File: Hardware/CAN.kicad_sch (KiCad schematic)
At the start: 10 parts, among them J8 Conn_01x02_Pin, U4 TCAN337, U5 CDSOT23-T24CAN

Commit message: small tweaks
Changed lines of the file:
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@@
 	)
 	(hierarchical_label "CAN_LOW"
-		(shape input)
+		(shape bidirectional)
 		(at 29.21 81.28 180)
 		(effects
@@
 	)
 	(hierarchical_label "CAN_LOW"
-		(shape input)
+		(shape bidirectional)
 		(at 63.5 43.18 0)
 		(effects
@@
 	)
 	(hierarchical_label "CAN_LOW"
-		(shape input)
+		(shape bidirectional)
 		(at 76.2 95.25 180)
 		(effects
@@
 	)
 	(hierarchical_label "CAN_HIGH"
-		(shape input)
+		(shape bidirectional)
 		(at 29.21 78.74 180)
 		(effects
@@
 	)
 	(hierarchical_label "CAN_RX"
-		(shape output)
+		(shape bidirectional)
 		(at 34.29 38.1 180)
 		(effects
@@
 	)
 	(hierarchical_label "CAN_TX"
-		(shape input)
+		(shape bidirectional)
 		(at 34.29 35.56 180)
 		(effects
@@
 	)
 	(hierarchical_label "CAN_HIGH"
-		(shape input)
+		(shape bidirectional)
 		(at 76.2 69.85 180)
 		(effects
@@
 	)
 	(hierarchical_label "CAN_TX"
-		(shape input)
+		(shape bidirectional)
 		(at 104.14 74.93 180)
 		(effects
@@
 	)
 	(hierarchical_label "CAN_RX"
-		(shape output)
+		(shape bidirectional)
 		(at 104.14 77.47 180)
 		(effects
@@
 	)
 	(hierarchical_label "CAN_HIGH"
-		(shape input)
+		(shape bidirectional)
 		(at 63.5 38.1 0)
 		(effects

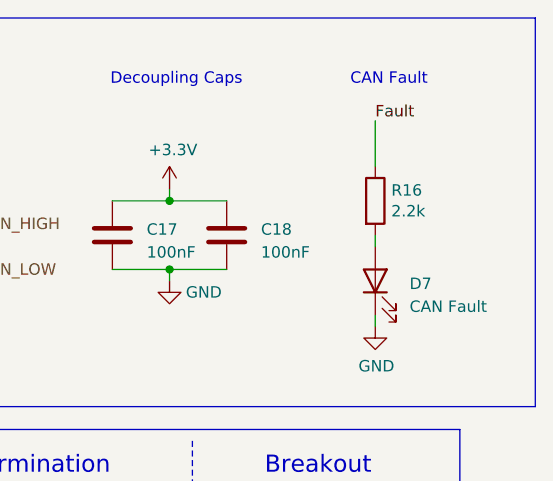
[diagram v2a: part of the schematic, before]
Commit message: new isolated amp, filter stage; need to select values
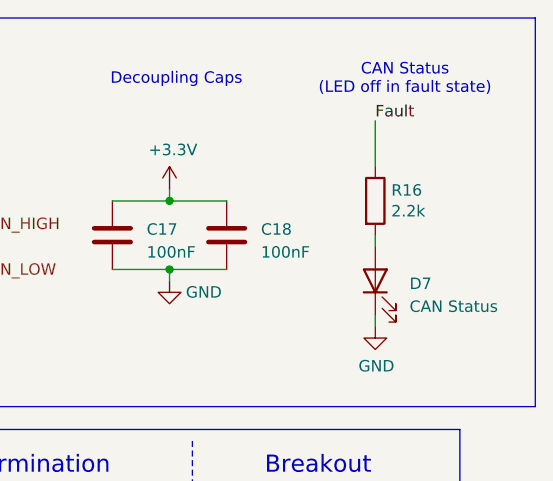
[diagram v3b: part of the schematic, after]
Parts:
- D7: value CAN Fault -> CAN Status
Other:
- note added: "CAN Status (LED off in fault state)"
- note removed: "CAN Fault"
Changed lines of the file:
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@@
 		)
 	)
-	(text "CAN Fault"
+	(text "CAN Status\n(LED off in fault state)"
 		(exclude_from_sim no)
-		(at 110.744 22.098 0)
-		(effects
-			(font
-				(size 1.27 1.27)
-			)
+		(at 112.522 20.32 0)
+		(effects
+			(font
+				(size 1.27 1.27)
+			)
+			(justify top)
 		)
 	)
@@
 			)
 		)
-		(property "Value" "CAN Fault"
+		(property "Value" "CAN Status"
 			(at 113.03 47.3074 90)
 			(effects

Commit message: lowk got some filter values from chat PLEASE PLEASE PLEASE VERIFY LATER
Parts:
- removed D7: CAN Status, LED_SMD:LED_0805_2012Metric, symbol Device:LED
- added D11: CAN Status, symbol Device:LED
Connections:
- net GND: now also D11.1 (K)
- net at R16.2: now also D11.2 (A)

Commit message: plz review
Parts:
- R16: value 2.2k -> ??
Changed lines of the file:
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@@
 			)
 		)
-		(property "Value" "2.2k"
+		(property "Value" "??"
 			(at 110.998 36.703 0)
 			(effects

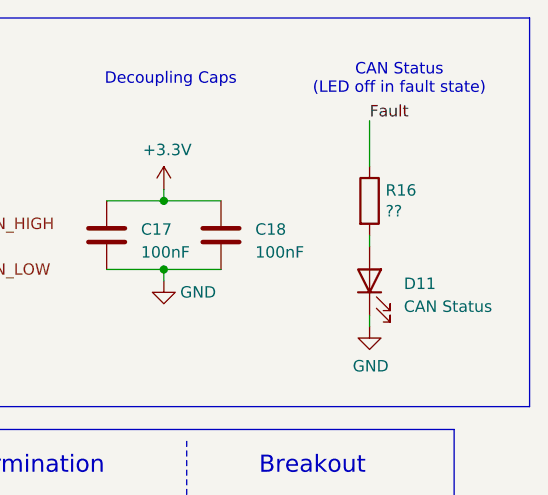
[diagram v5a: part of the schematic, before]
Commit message: added LEDs, changed LDO, still need to address other comments
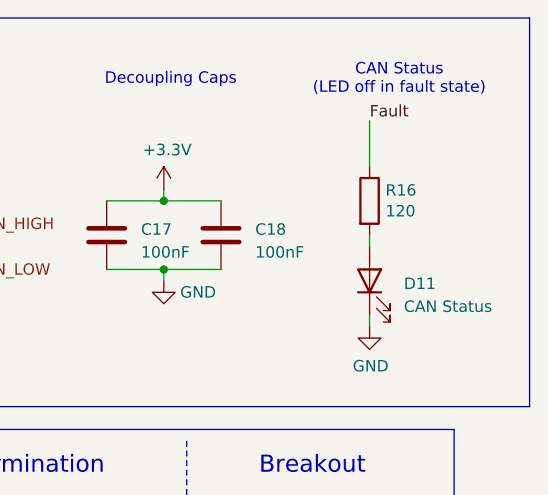
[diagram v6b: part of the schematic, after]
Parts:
- R16: value ?? -> 120
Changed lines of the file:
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@@
 			)
 		)
-		(property "Value" "??"
+		(property "Value" "120"
 			(at 110.998 36.703 0)
 			(effects

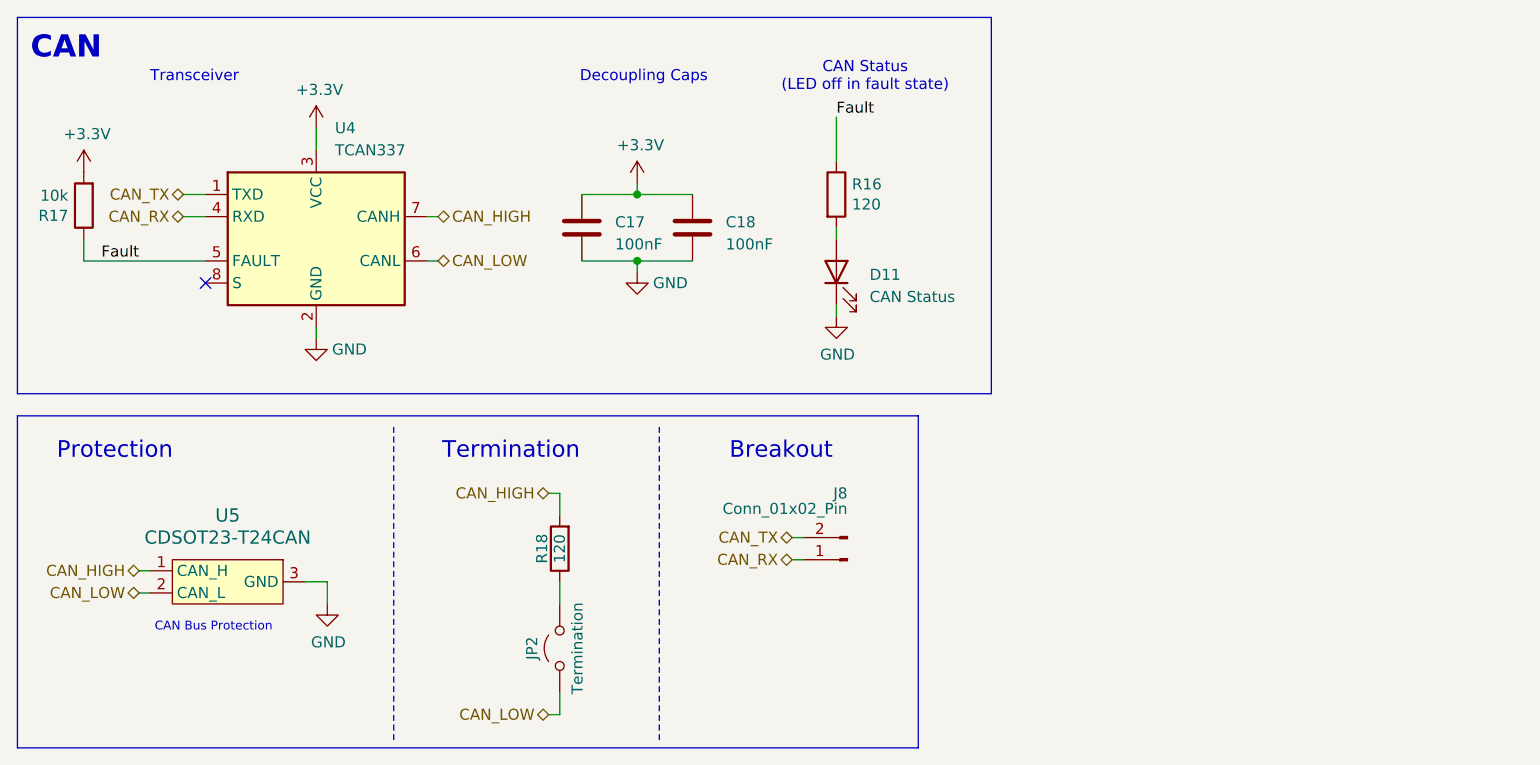
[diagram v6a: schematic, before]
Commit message: scrutineering should be done, started on USB
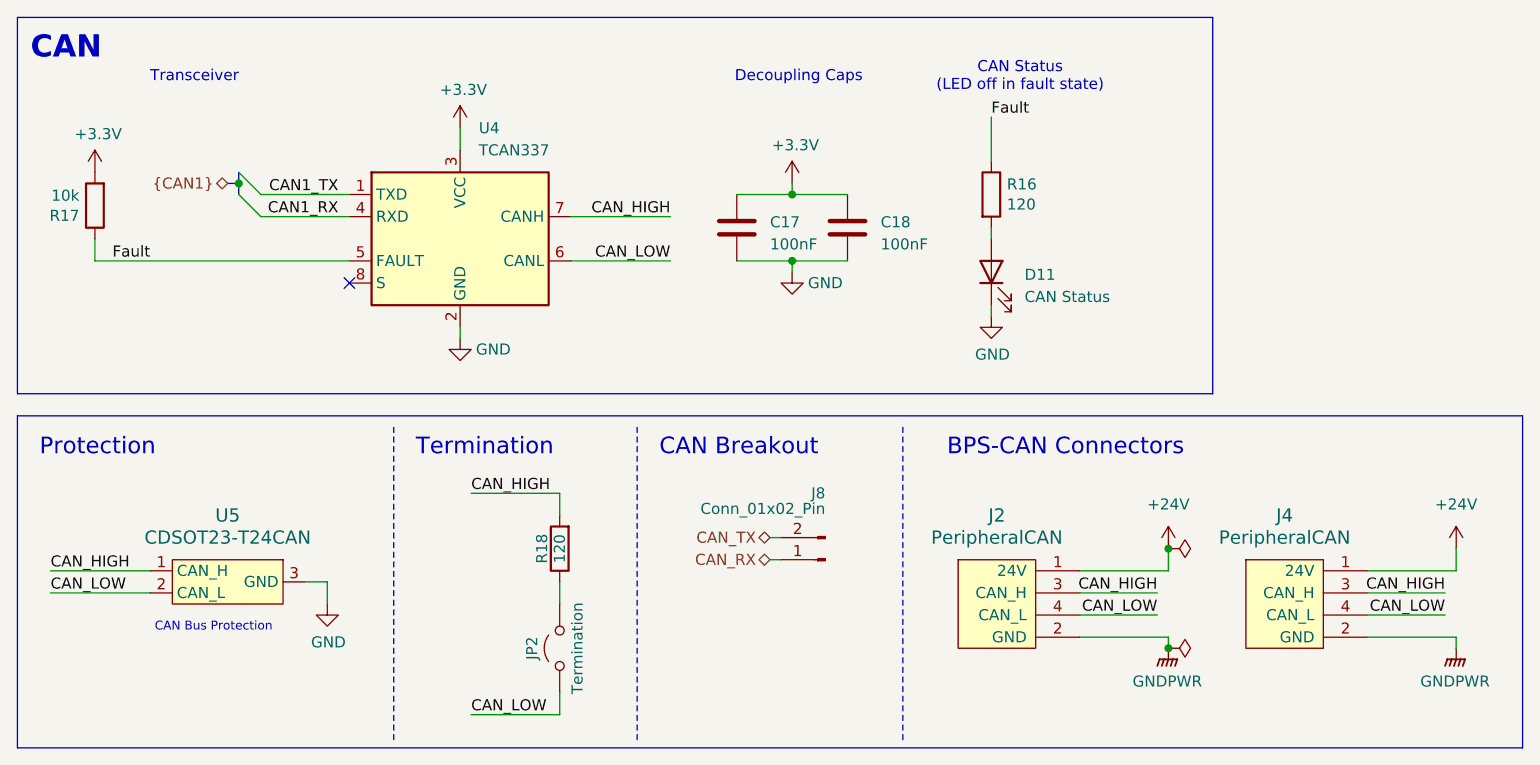
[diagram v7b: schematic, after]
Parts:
- added J2, J4: PeripheralCAN, UTSVT_Connectors:Molex_Nano-Fit_105309-xx04_1x04_P2.50mm_Vertical, symbol utsvt-connectors:PeripheralCANConnector
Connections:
- net CAN_HIGH: now also J2.3 (CAN_H), J4.3 (CAN_H)
- net CAN_LOW: now also J2.4 (CAN_L), J4.4 (CAN_L)
- net CAN_RX: no longer U4.4 (RXD)
- net CAN_TX: no longer U4.1 (TXD)
- new net +24V: J2.1 (24V), J4.1 (24V)
- new net CAN1_RX: U4.4 (RXD)
- new net CAN1_TX: U4.1 (TXD)
- new net GNDPWR: J2.2 (GND), J4.2 (GND)
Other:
- note added: "BPS-CAN Connectors"
- note added: "CAN Breakout"
- note removed: "Breakout"
- moved on the sheet: C17, C18, D11, J8, R16, R17, U4

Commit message: copied USB-C from psom
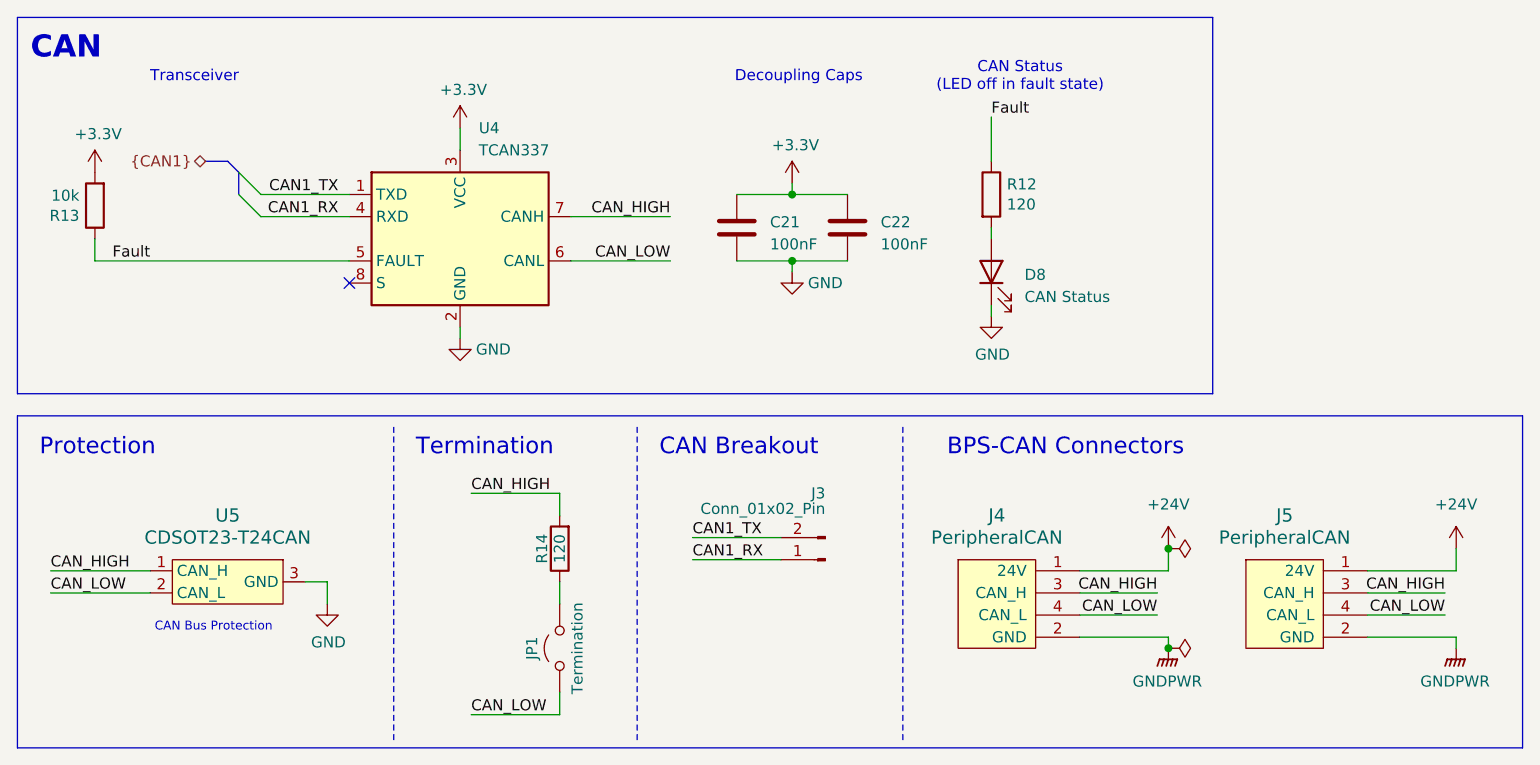
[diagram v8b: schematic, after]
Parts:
- renumbered C17 to C21, C18 to C22, D11 to D8, J8 to J3, J2 to J4, J4 to J5, JP2 to JP1, R16 to R12, R17 to R13, R18 to R14
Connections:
- net CAN_RX is gone; now on net CAN1_RX: J3.1 (Pin_1)
- net CAN_TX is gone; now on net CAN1_TX: J3.2 (Pin_2)
